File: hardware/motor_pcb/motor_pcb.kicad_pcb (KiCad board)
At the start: 2 copper layers, 14 parts, among them J1 PWR, J2 Conn_01x03, J3 Conn_01x12, U1 TMC6300, U2 MT6701-CT

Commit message: Updated design with new wiring structure
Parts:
- added H1: MountingHole, Holes:Holes, F.Cu at (50.0, 50.0)
- added TP1: 3V3, TestPoint:TestPoint_Pad_2.0x2.0mm, B.Cu at (50.0, 66.5)
- added TP2: BLK, TestPoint:TestPoint_Pad_2.0x2.0mm, B.Cu at (45.7, 65.9)
- added TP3: DC, TestPoint:TestPoint_Pad_2.0x2.0mm, B.Cu at (41.8, 64.3)
- added TP4: CS, TestPoint:TestPoint_Pad_2.0x2.0mm, B.Cu at (38.3, 61.7)
- added TP5: SCL, TestPoint:TestPoint_Pad_2.0x2.0mm, B.Cu at (35.7, 58.2)
- added TP6: SDA, TestPoint:TestPoint_Pad_2.0x2.0mm, B.Cu at (34.1, 54.3)
- added TP7: RES, TestPoint:TestPoint_Pad_2.0x2.0mm, B.Cu at (33.5, 50.0)
- added TP8: GND, TestPoint:TestPoint_Pad_2.0x2.0mm, B.Cu at (34.1, 45.7)
- J1: value PWR -> Conn_01x14; footprint Connector_PinHeader_2.54mm:PinHeader_1x02_P2.54mm_Vertical -> Connector_Hirose:Hirose_DF52-14S-0.8H_1x14-1MP_P0.80mm_Horizontal
- J2: moved to B.Cu
- J3: value Conn_01x12 -> Conn_01x14; footprint Jushuo:FPC_12 -> Connector_Hirose:Hirose_DF52-14S-0.8H_1x14-1MP_P0.80mm_Horizontal
- moved C1 1172.7 mm to (91.5, 75.1)
- moved C2 1172.7 mm to (108.6, 64.5)
- moved C3 1172.7 mm to (95.8, 74.8)
- moved C4 1172.7 mm to (101.2, 69.2)
- moved C5 1172.7 mm to (105.2, 67.3)
- moved C6 1172.7 mm to (99.8, 74.8)
- moved R1 1172.7 mm to (86.5, 75.1)
- moved R2 1172.7 mm to (108.6, 62.0)
- moved R3 1172.7 mm to (101.2, 71.7)
- moved U2 1139.0 mm to (50.0, 50.0)
- moved J1 1138.5 mm to (60.0, 40.0), turned to -45 degrees
- moved J2 1136.4 mm to (57.2, 61.8), turned to -135 degrees
- moved J3 1127.4 mm to (40.0, 40.0), turned to 45 degrees
- moved U1 1113.7 mm to (43.5, 60.0), turned to 90 degrees
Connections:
- J1 pad 1: GND -> +5V
- J3 pad 10: /SCL -> /SDA
- J3 pad 11: /CS -> /SCL
- J3 pad 2: /UH -> +3V3
- J3 pad 3: /UL -> /UH
- J3 pad 4: /VH -> /UL
- J3 pad 5: /VL -> /VH
- J3 pad 6: /WH -> /VL
- J3 pad 7: /WL -> /WH
- J3 pad 8: /DIAG -> /WL
- J3 pad 9: /SDA -> /DIAG
- U2 pad 8: /CS -> +3V3
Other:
- board outline added: 36 x 36 mm

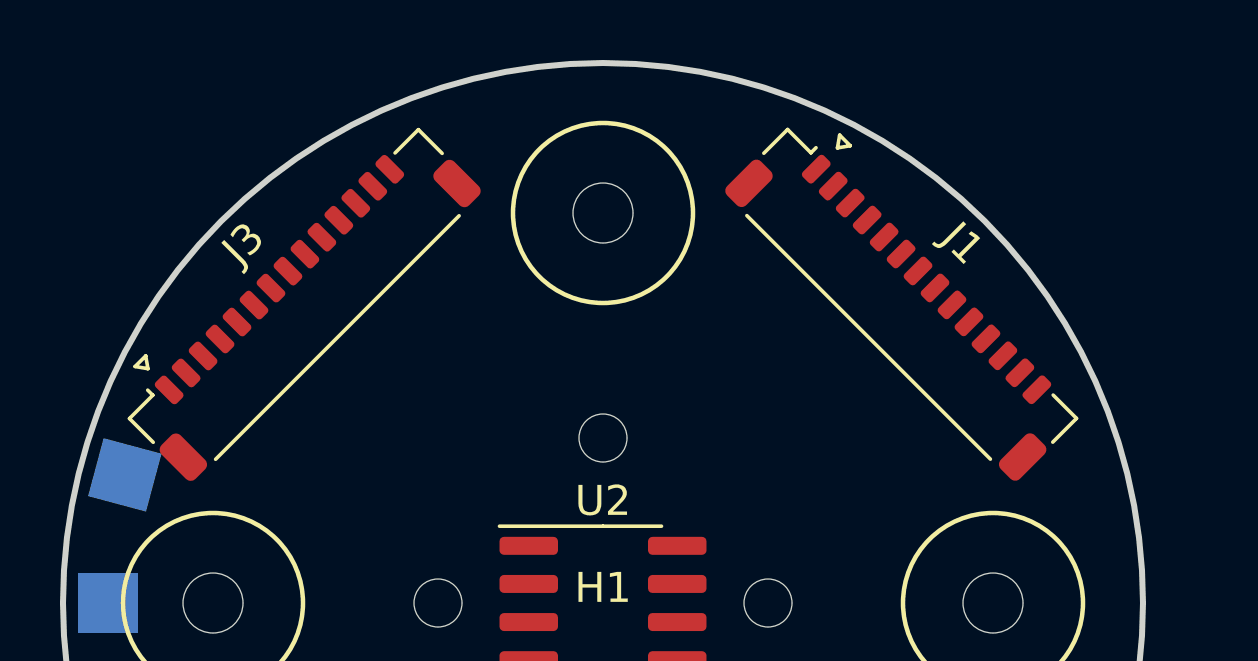
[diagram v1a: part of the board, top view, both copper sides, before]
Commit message: Updated connectors
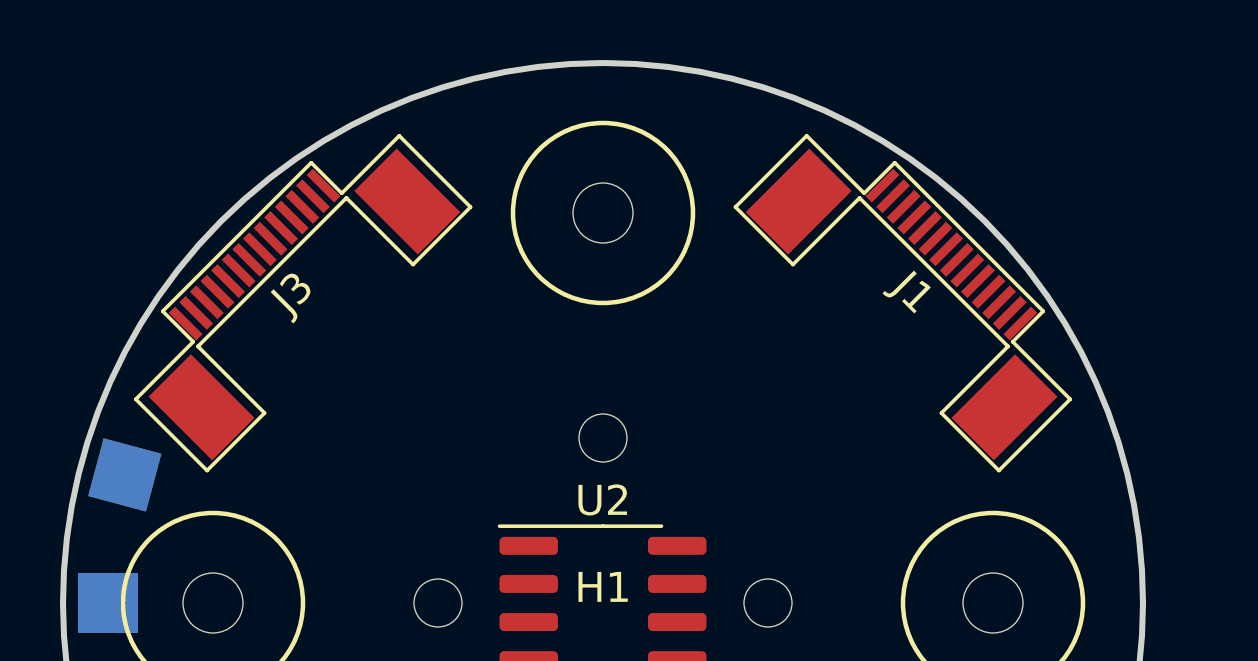
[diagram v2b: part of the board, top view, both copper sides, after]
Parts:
- J1, J3: footprint Connector_Hirose:Hirose_DF52-14S-0.8H_1x14-1MP_P0.80mm_Horizontal -> Jushuo:FPC_14
- moved J3 2.29 mm to (38.4, 38.4)
- moved J1 2.28 mm to (61.6, 38.4)

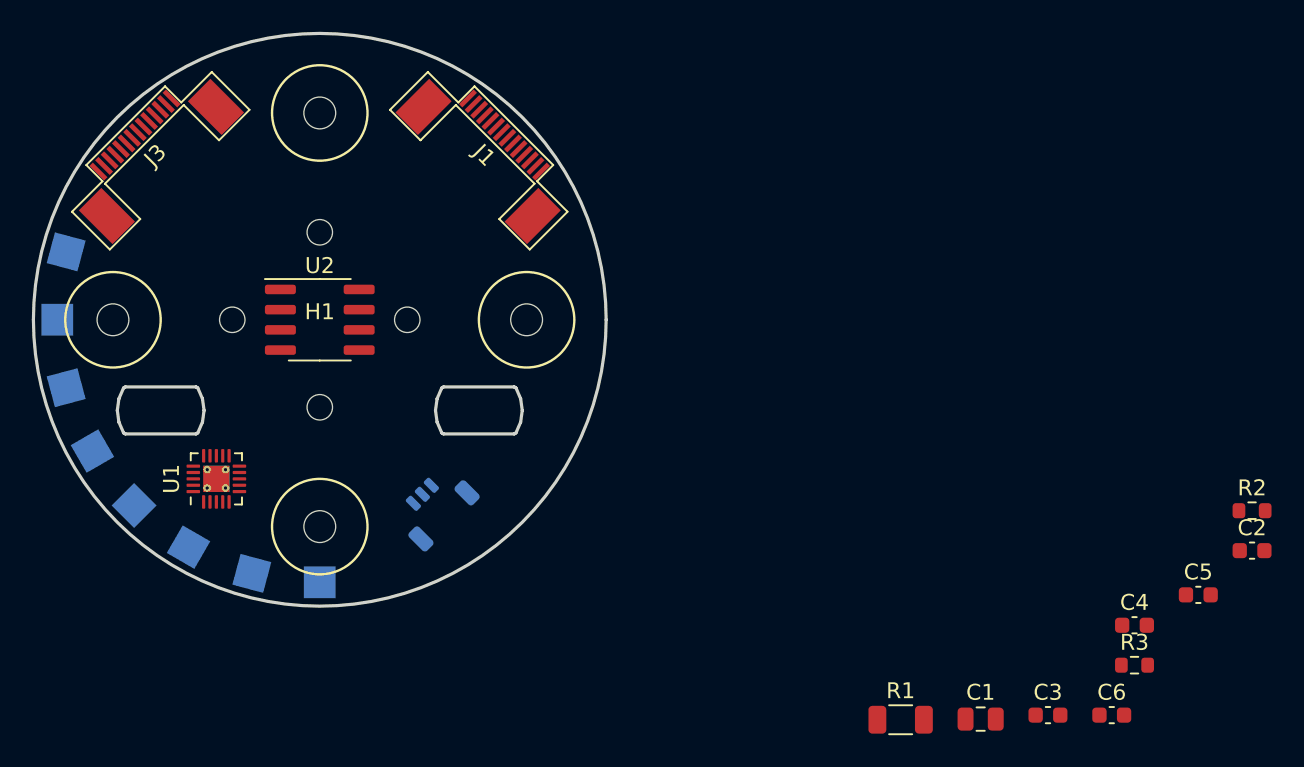
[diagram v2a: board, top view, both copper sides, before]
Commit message: Routed motor pcb
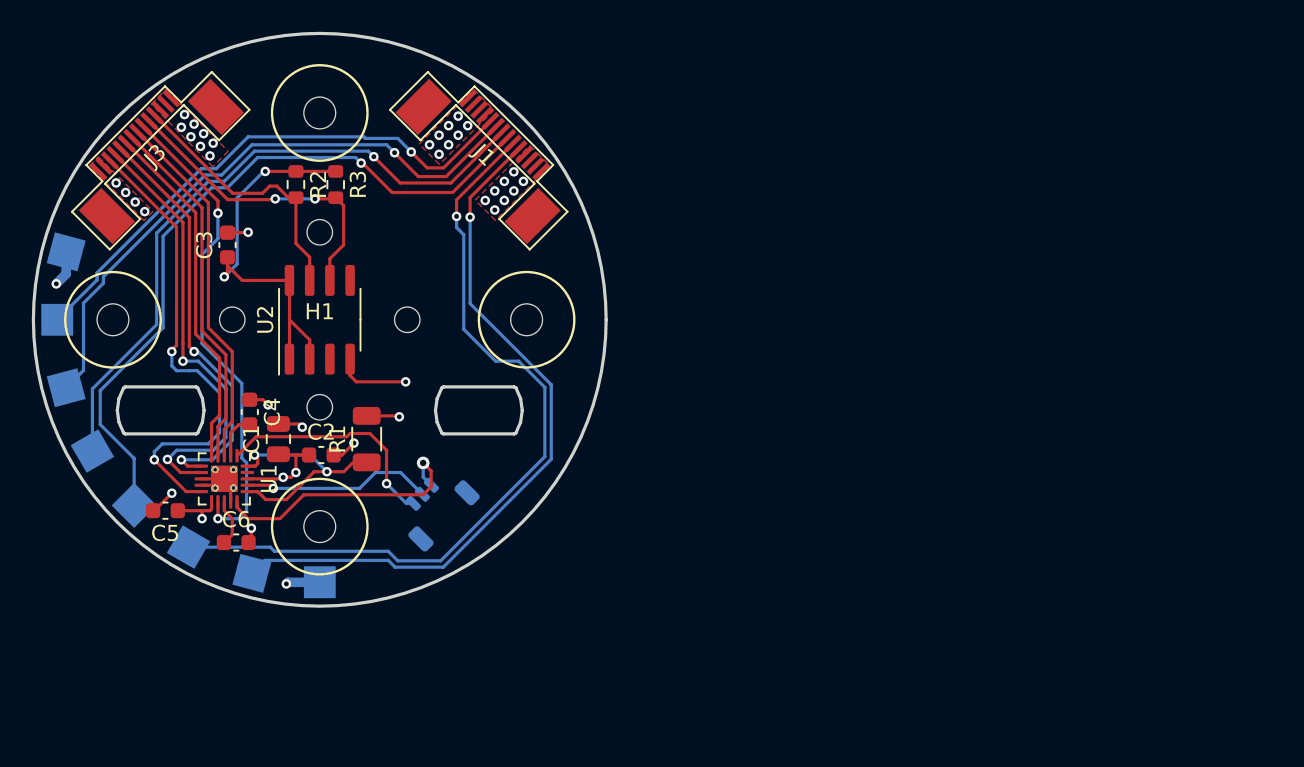
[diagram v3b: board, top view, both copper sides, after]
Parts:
- moved C5 65.1 mm to (40.3, 62.0), turned to 180 degrees
- moved R2 63.5 mm to (48.5, 41.5), turned to -90 degrees
- moved C3 59.4 mm to (44.2, 45.3), turned to 90 degrees
- moved C2 58.8 mm to (50.1, 58.5)
- moved R3 58.6 mm to (51.0, 41.5), turned to -90 degrees
- moved C4 57.2 mm to (45.6, 55.8), turned to -90 degrees
- moved C6 56.1 mm to (44.8, 64.0)
- moved C1 47.5 mm to (47.4, 57.5), turned to 90 degrees
- moved R1 37.9 mm to (53.0, 57.5), turned to 90 degrees
- moved U1 0.50 mm to (44.0, 60.0), turned to -90 degrees
- turned U2 to 90 degrees
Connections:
- J3 pad 3: /UH -> /VL
- J3 pad 4: /UL -> /WL
- J3 pad 5: /VH -> /UL
- J3 pad 6: /VL -> /WH
- J3 pad 7: /WH -> /VH
- J3 pad 8: /WL -> /UH
- TP2 pad 1: Net-(J1-Pad5) -> Net-(J1-Pad10)
- TP3 pad 1: Net-(J1-Pad6) -> Net-(J1-Pad9)
- TP4 pad 1: Net-(J1-Pad7) -> Net-(J1-Pad8)
- TP5 pad 1: Net-(J1-Pad8) -> Net-(J1-Pad7)
- TP6 pad 1: Net-(J1-Pad9) -> Net-(J1-Pad6)
- TP7 pad 1: Net-(J1-Pad10) -> Net-(J1-Pad5)
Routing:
- net +3V3: track 0.00 -> 77.6 mm, vias 0 -> 8
- net Net-(J1-Pad9): track 0.00 -> 49.8 mm, vias 0 -> 1
- net Net-(J1-Pad8): track 0.00 -> 45.5 mm, vias 0 -> 1
- net Net-(J1-Pad10): track 0.00 -> 45.0 mm, vias 0 -> 1
- net Net-(J1-Pad7): track 0.00 -> 41.3 mm, vias 0 -> 1
- net Net-(J1-Pad6): track 0.00 -> 38.2 mm, vias 0 -> 1
- net Net-(J1-Pad5): track 0.00 -> 34.3 mm, vias 0 -> 1
- net /DIAG: track 0.00 -> 30.7 mm, vias 0 -> 2
- net /VL: track 0.00 -> 29.9 mm, vias 0 -> 2
- net /WL: track 0.00 -> 27.9 mm, vias 0 -> 2
- net /UL: track 0.00 -> 26.5 mm, vias 0 -> 2
- net /UH: track 0.00 -> 23.0 mm
- net /VH: track 0.00 -> 22.6 mm
- net /WH: track 0.00 -> 22.3 mm
- net /SDA: track 0.00 -> 19.6 mm, vias 0 -> 2
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- added copper zone on F.Cu, net +3V3
- added copper zone on F.Cu, net +5V
- added copper zone on In2.Cu, net +5V
- added copper zone on F.Cu, net GND
- added copper zone on In1.Cu, net GND
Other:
- copper layers 2 -> 4
